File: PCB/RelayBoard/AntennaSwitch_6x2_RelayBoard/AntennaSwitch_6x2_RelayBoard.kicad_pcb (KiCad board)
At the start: 2 copper layers, 200 x 105 mm, 34 parts, among them J1 Conn_Coaxial, J10 Conn_01x08, J2 Conn_Coaxial, J3 Conn_Coaxial, J4 Conn_Coaxial, J5 Conn_Coaxial, J6 Conn_Coaxial, J7 Conn_Coaxial, J8 Conn_Coaxial, J9 Conn_01x08, K1 FINDER-40.61, K10 FINDER-40.61, K11 FINDER-40.61, K12 FINDER-40.61, K13 FINDER-40.61, K14 FINDER-40.61, K15 FINDER-40.61, K16 FINDER-40.61, K17 FINDER-40.61, K18 FINDER-40.61, K2 FINDER-40.61, K3 FINDER-40.61, K4 FINDER-40.61, K5 FINDER-40.61, K6 FINDER-40.61, K7 FINDER-40.61, K8 FINDER-40.61, K9 FINDER-40.61, U1 ULN2003, U2 ULN2003, U3 74HC04, U4 74HC04

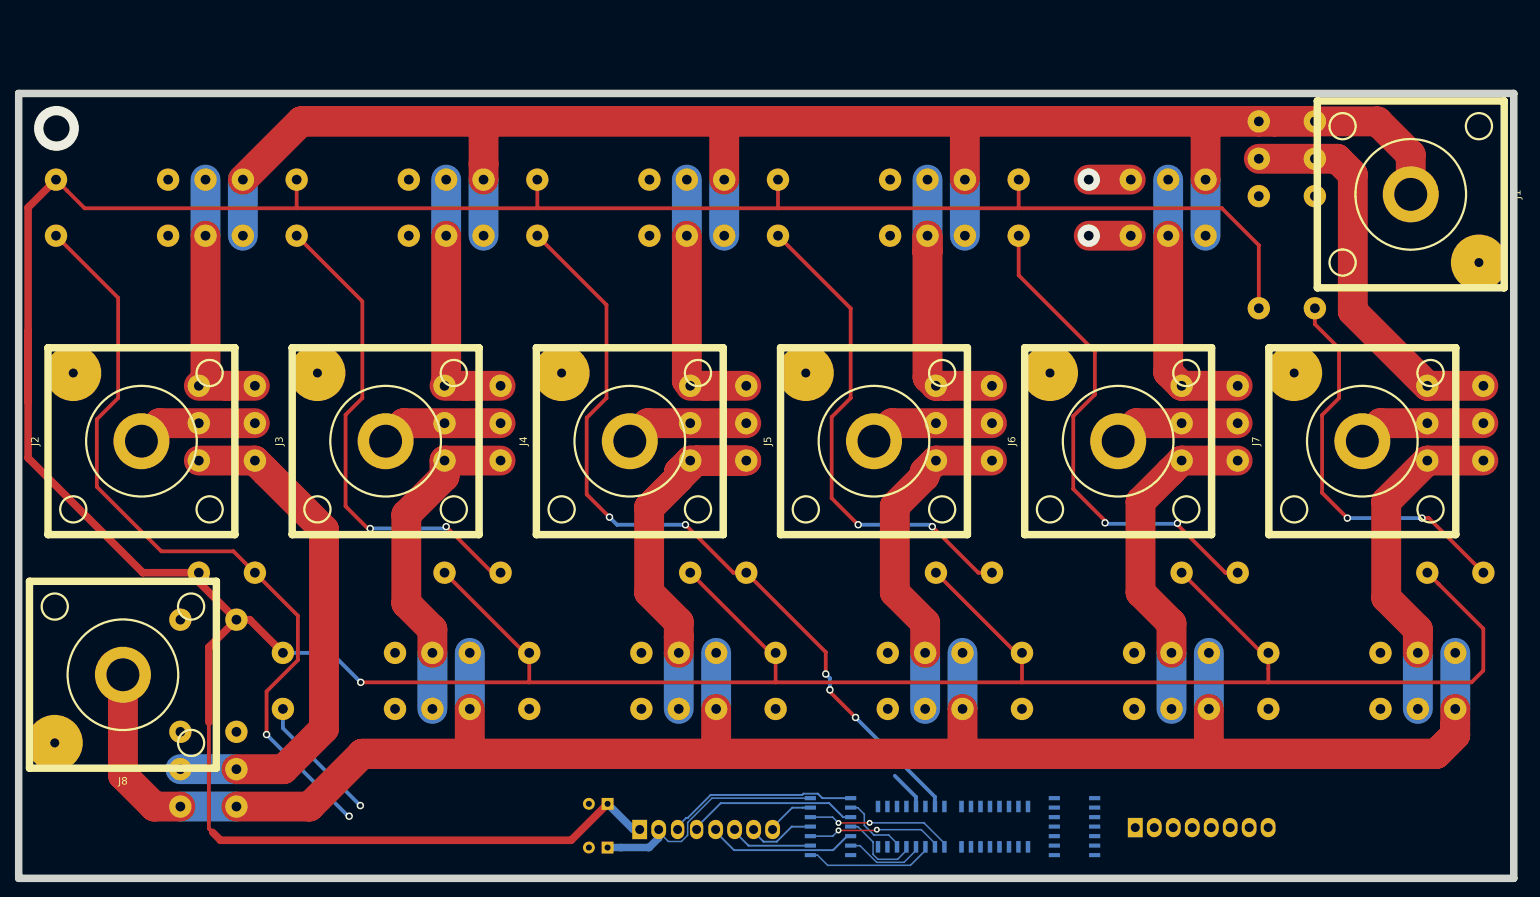
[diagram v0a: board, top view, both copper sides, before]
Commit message: Relay Board PCB first draft
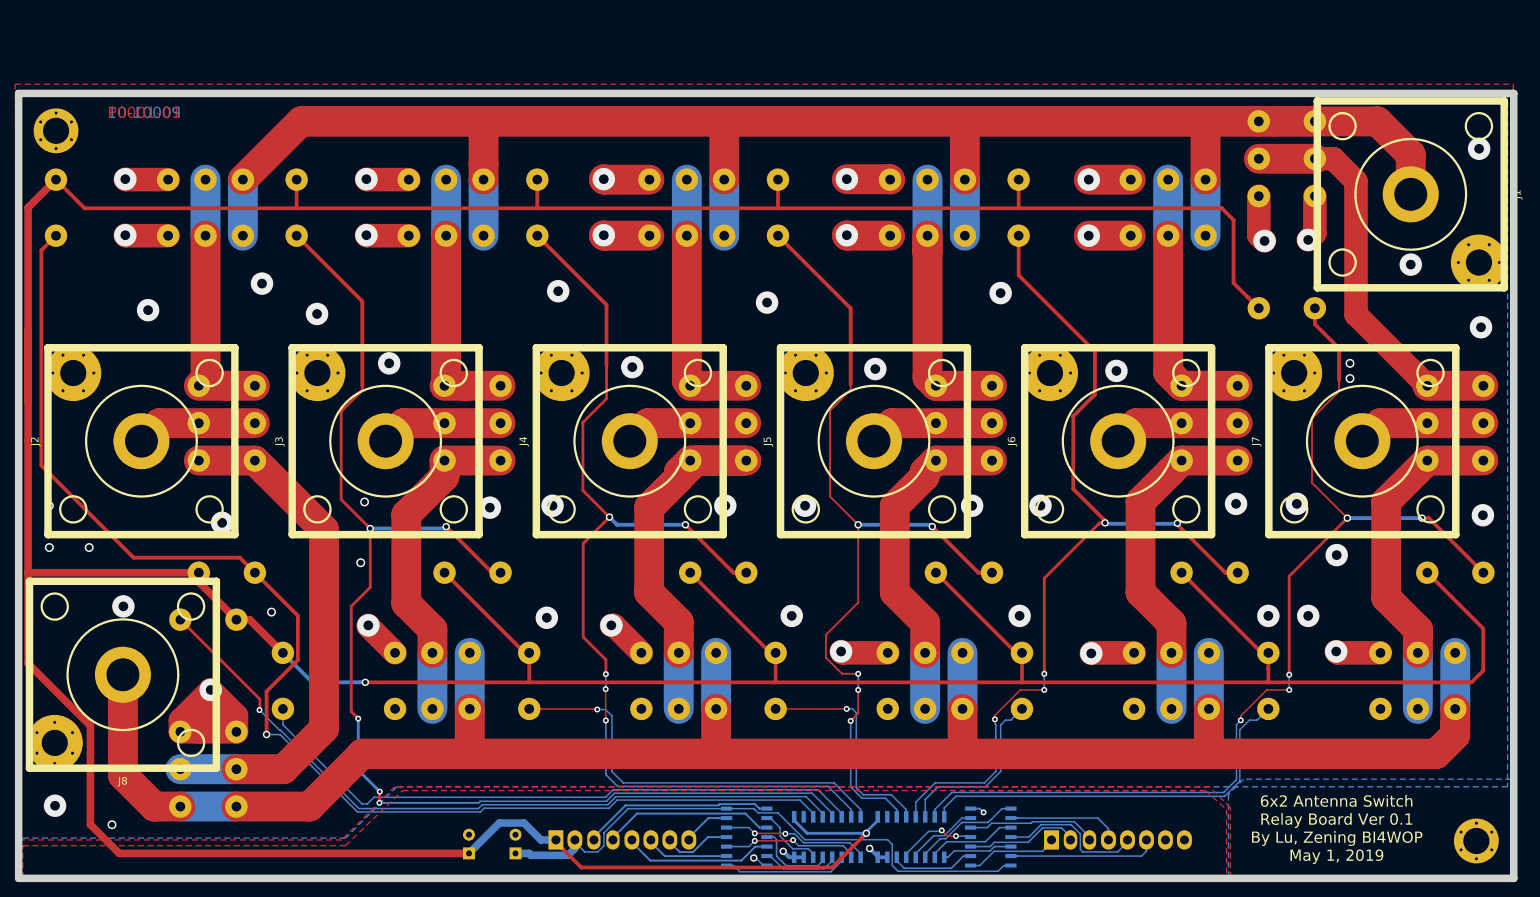
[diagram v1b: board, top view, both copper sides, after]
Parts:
- added REF**: M3_Screwhole, MyPCBLib:M3_Screwhole, F.Cu at (245.0, 150.0)
- added REF**: M3_Screwhole, MyPCBLib:M3_Screwhole, F.Cu at (55.0, 55.0)
- moved C1 19.7 mm to (110.2, 151.7), turned to 90 degrees
- moved C2 12.3 mm to (116.5, 151.7), turned to 90 degrees
- moved B 11.3 mm to (188.2, 149.9)
- moved A 11.3 mm to (121.9, 149.9)
- moved U2 11.3 mm to (169.4, 149.5)
- moved U3 11.3 mm to (147.4, 149.5)
- moved U4 11.3 mm to (180.0, 149.5)
- moved U1 11.3 mm to (158.2, 149.5)
- renumbered J9 to A, J10 to B
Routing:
- net GNDPWR: track 11.3 -> 133.7 mm, vias 2 -> 84
- net Net-(K13-PadA1): track 0.00 -> 99.4 mm, vias 0 -> 1
- net Net-(K2-PadA1): track 70.7 -> 168.4 mm, vias 2 -> 5
- net Net-(K12-PadA1): track 53.0 -> 140.0 mm, vias 2 -> 5
- net +12V: track 638.0 -> 712.1 mm, vias 1 -> 2
- net Net-(K14-PadA1): track 17.2 -> 83.8 mm, vias 1 -> 0
- net Net-(K1-PadA1): track 105.5 -> 171.1 mm, vias 2 -> 1
- net Net-(K11-PadA1): track 66.3 -> 122.4 mm, vias 2 -> 5
- net Net-(K15-PadA1): track 0.00 -> 55.3 mm, vias 0 -> 1
- net Net-(K18-PadA1): track 0.00 -> 54.1 mm
- net Net-(K10-PadA1): track 65.8 -> 114.7 mm, vias 2 -> 5
- net +3V3: track 33.0 -> 77.6 mm
- net Net-(K3-PadA1): track 106.9 -> 138.5 mm
- net Net-(K16-PadA1): track 0.00 -> 29.9 mm, vias 0 -> 1
- net Net-(K17-PadA1): track 0.00 -> 23.9 mm
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- added copper zone on F.Cu, net GND
- added copper zone on B.Cu, net GNDPWR
- added copper zone on F.Cu, net GNDPWR
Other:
- board text added: "12V"
- board text added: "3.3V"
- board text added: "6x2 Antenna Switch Relay Board Ver 0.1 By Lu, Zening BI4WOP May 1, 2019"
- board text added: "Inputs are LOW effective"
- board text added: "P0001-01"
- board text added: "Rated RF Power: 1500W Rated Frequency: 1.8MHz-30MHz"
- board text added: "Relays: Finder 40.61.7.012"
- board text added: "SEL1_1"
- board text added: "SEL1_6"
- board text added: "SEL2_1"
- board text added: "SEL2_6"
- board text added: "SGND"

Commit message: FS Tools
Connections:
- REF** pad 1: A -> GNDPWR
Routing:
- net B: track 409.6 -> 272.4 mm
- net A: track 533.8 -> 582.2 mm
- net GNDPWR: track 133.7 -> 152.1 mm, vias 84 -> 101
- net +12V: track 712.1 -> 705.1 mm
- net Net-(K1-PadA1): track 171.1 -> 177.0 mm
- net Net-(K2-PadA1): track 168.4 -> 173.7 mm
- net Net-(K13-PadA1): track 99.4 -> 103.4 mm
- net Net-(K14-PadA1): track 83.8 -> 86.6 mm
- net Net-(K10-PadA1): track 114.7 -> 115.8 mm
- net GND: track 12.7 -> 13.2 mm, vias 4 -> 5
- added copper zone on F.Cu, net A
- added copper zone on F.Cu, net B
- added copper zone on F.Cu, net Net-(K1-Pad11)
- added copper zone on F.Cu, net Net-(K10-Pad12)
- added copper zone on F.Cu, net Net-(K10-Pad14)
- added copper zone on F.Cu, net Net-(K11-Pad12)
- added copper zone on F.Cu, net Net-(K11-Pad14)
- added copper zone on F.Cu, net Net-(K12-Pad12)
- added copper zone on F.Cu, net Net-(K12-Pad14)
- added copper zone on F.Cu, net Net-(K13-Pad11)
- added copper zone on F.Cu, net Net-(K14-Pad11)
- added copper zone on F.Cu, net Net-(K15-Pad11)
- added copper zone on F.Cu, net Net-(K2-Pad11)
- added copper zone on F.Cu, net Net-(K3-Pad11)
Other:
- board size 200 x 105 mm -> 200 x 115 mm
- net class RF: clearance 2 -> 1.5

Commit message: New control board design
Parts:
- removed A, B: Conn_01x08, Connectors_Molex:Molex_KK-6410-08_08x2.54mm_Straight
- removed C1, C2: 100uF, Capacitors_THT:CP_Radial_D5.0mm_P2.50mm
- removed J1, J2, J3, J4, J5, J6, J7, J8: Conn_Coaxial, MyPCBLib:SL16_Screw_PCB
- removed K1, K10, K11, K12, K13, K14, K15, K16, K17, K18, K2, K3, K4, K5, K6, K7, K8, K9: FINDER-40.61, MyPCBLib:Finder_40.61
- removed REF** (x2): M3_Screwhole, MyPCBLib:M3_Screwhole
- removed U1, U2: ULN2003, digikey-footprints:SOIC-16_W3.90mm
- removed U3, U4: 74HC04, digikey-footprints:SOIC-14_W3.9mm
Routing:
- net +12V: track 705.1 -> 0.00 mm, vias 2 -> 0
- net A: track 582.2 -> 0.00 mm
- net B: track 272.4 -> 0.00 mm
- net Net-(K1-PadA1): track 177.0 -> 0.00 mm, vias 1 -> 0
- net Net-(K2-PadA1): track 173.7 -> 0.00 mm, vias 5 -> 0
- net GNDPWR: track 152.1 -> 0.00 mm, vias 101 -> 0
- net Net-(K12-PadA1): track 140.1 -> 0.00 mm, vias 5 -> 0
- net Net-(K3-PadA1): track 138.6 -> 0.00 mm, vias 5 -> 0
- net Net-(K11-PadA1): track 122.4 -> 0.00 mm, vias 5 -> 0
- net Net-(K10-PadA1): track 115.8 -> 0.00 mm, vias 5 -> 0
- net Net-(K13-PadA1): track 103.4 -> 0.00 mm, vias 1 -> 0
- net Net-(K14-PadA1): track 86.6 -> 0.00 mm
- net +3V3: track 77.6 -> 0.00 mm
- net Net-(K13-Pad11): track 68.6 -> 0.00 mm
- net Net-(K15-Pad11): track 60.3 -> 0.00 mm
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- removed copper zone on F.Cu, net A
- removed copper zone on F.Cu, net B
- removed copper zone on F.Cu, net GND
- removed copper zone on B.Cu, net GNDPWR
- removed copper zone on F.Cu, net GNDPWR
- removed copper zone on F.Cu, net Net-(K1-Pad11)
- removed copper zone on F.Cu, net Net-(K10-Pad12)
- removed copper zone on F.Cu, net Net-(K10-Pad14)
- removed copper zone on F.Cu, net Net-(K11-Pad12)
- removed copper zone on F.Cu, net Net-(K11-Pad14)
- removed copper zone on F.Cu, net Net-(K12-Pad12)
- removed copper zone on F.Cu, net Net-(K12-Pad14)
- removed copper zone on F.Cu, net Net-(K13-Pad11)
- removed copper zone on F.Cu, net Net-(K14-Pad11)
- removed copper zone on F.Cu, net Net-(K15-Pad11)
- removed copper zone on F.Cu, net Net-(K2-Pad11)
- removed copper zone on F.Cu, net Net-(K3-Pad11)
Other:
- board outline removed
- board text removed: "12V"
- board text removed: "3.3V"
- board text removed: "6x2 Antenna Switch Relay Board Ver 0.1 By Lu, Zening BI4WOP May 1, 2019"
- board text removed: "Inputs are LOW effective"
- board text removed: "P0001-01"
- board text removed: "Rated RF Power: 1500W Rated Frequency: 1.8MHz-30MHz"
- board text removed: "Relays: Finder 40.61.7.012"
- board text removed: "SEL1_1"
- board text removed: "SEL1_6"
- board text removed: "SEL2_1"
- board text removed: "SEL2_6"
- board text removed: "SGND"
